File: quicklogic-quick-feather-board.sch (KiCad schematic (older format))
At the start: 50 parts, among them IC1 EOS-S3, J5 0473460001, Q1 BSS138AKA, Q2 BSS84, U1 TPS62821DLCR, U2 MCP73831T-2ACI_OT, U3 GD25Q16CWIGR, U4 DPS310, U5 MC3635, X1 ECS-_327-12_5-34B-TR

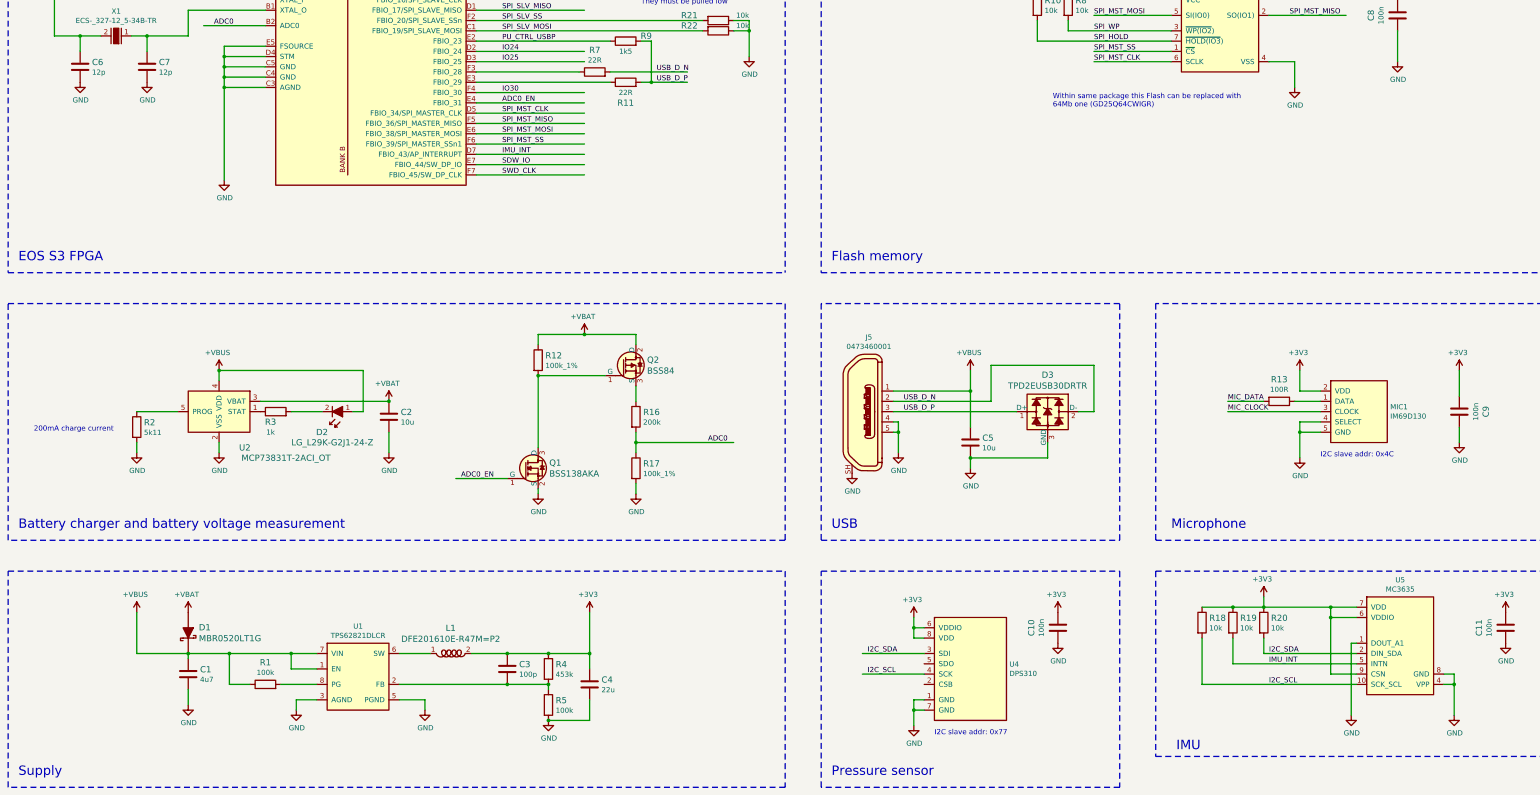
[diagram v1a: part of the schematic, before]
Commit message: Added remarks about power consuption, added filtering capactitors for EOS-S3
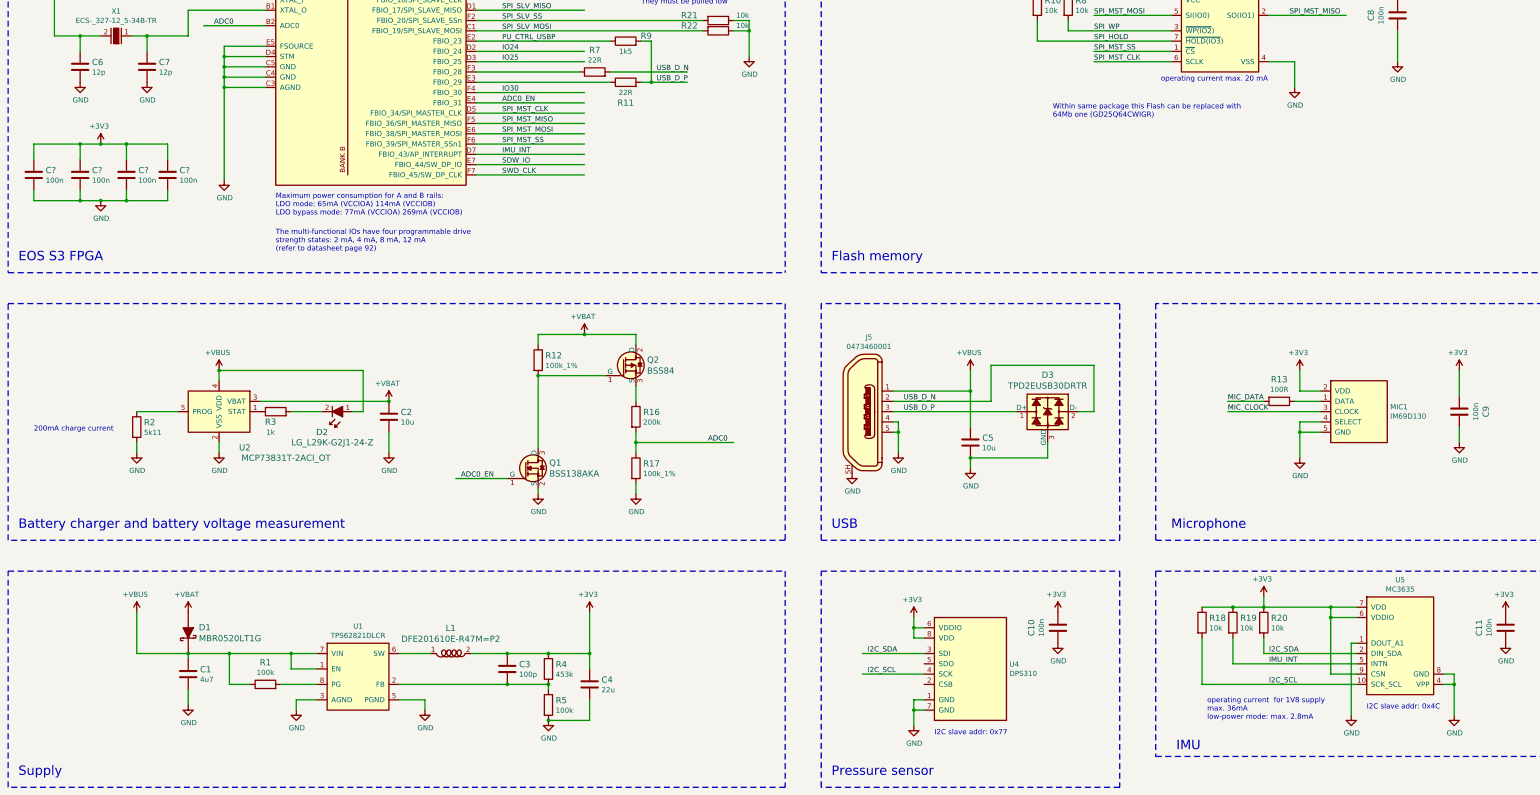
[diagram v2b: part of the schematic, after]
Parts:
- added C? (x4): C_100n_0402_6V3, antmicro-footprints:0402-cap, symbol antmicroCapacitors0402:C_100n_0402_6V3
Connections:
- wire segments 198 -> 214
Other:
- note added: "Maximum power consumption for A and B rails:\nLDO mode: 65mA (VCCIOA) 114mA (VCCIOB)\nLDO bypass mode: 77mA (VCCIOA) 269mA (VCCIOB)"
- note added: "The multi-functional IOs have four programmable drive \nstrength states: 2 mA, 4 mA, 8 mA, 12 mA \n(refer to datasheet page 92)"
- note added: "operating current for 1V8 supply\nmax. 36mA\nlow-power mode: max. 2.8mA"
- note added: "operating current max. 20 mA"
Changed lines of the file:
@@
 Wire Wire Line
 	11250 3050 12000 3050
-Text Notes 10850 3600 0    50   ~ 0
+Text Notes 10850 3700 0    50   ~ 0
 Within same package this Flash can be replaced with \n64Mb one (GD25Q64CWIGR)
 Wire Wire Line
@@
 Wire Wire Line
 	9600 9100 9000 9100
-Text Notes 13450 7000 0    50   ~ 0
+Text Notes 13900 9450 0    50   ~ 0
 I2C slave addr: 0x4C
 Text Notes 9700 9700 0    50   ~ 0
@@
 $EndComp
 Connection ~ 4400 6450
+Text Notes 3300 4650 0    50   ~ 0
+Maximum power consumption for A and B rails:\nLDO mode: 65mA (VCCIOA) 114mA (VCCIOB)\nLDO bypass mode: 77mA (VCCIOA) 269mA (VCCIOB)
+$Comp
+L antmicroCapacitors0402:C_100n_0402_6V3 C?
+U 1 1 5DDEA3A8
+P 950 4250
+F 0 "C?" H 1065 4295 60  0000 L CNN
+F 1 "C_100n_0402_6V3" H 950 4100 60  0001 C CNN
+F 2 "antmicro-footprints:0402-cap" H 1150 4450 60  0001 L CNN
+F 3 "" H 950 4250 50  0001 C CNN
+F 4 "Walsin" H 1150 4650 60  0001 L CNN "Manufacturer"
+F 5 "0402X104K6R3CT" H 1150 4550 60  0001 L CNN "MPN"
+F 6 "100n" H 1065 4197 50  0000 L CNN "Val"
+	1    950  4250
+	1    0    0    -1
+$EndComp
+$Comp
+L antmicroCapacitors0402:C_100n_0402_6V3 C?
+U 1 1 5DDEA7E7
+P 1400 4250
+F 0 "C?" H 1515 4295 60  0000 L CNN
+F 1 "C_100n_0402_6V3" H 1400 4100 60  0001 C CNN
+F 2 "antmicro-footprints:0402-cap" H 1600 4450 60  0001 L CNN
+F 3 "" H 1400 4250 50  0001 C CNN
+F 4 "Walsin" H 1600 4650 60  0001 L CNN "Manufacturer"
+F 5 "0402X104K6R3CT" H 1600 4550 60  0001 L CNN "MPN"
+F 6 "100n" H 1515 4197 50  0000 L CNN "Val"
+	1    1400 4250
+	1    0    0    -1
+$EndComp
+$Comp
+L antmicroCapacitors0402:C_100n_0402_6V3 C?
+U 1 1 5DDEACD8
+P 1850 4250
+F 0 "C?" H 1965 4295 60  0000 L CNN
+F 1 "C_100n_0402_6V3" H 1850 4100 60  0001 C CNN
+F 2 "antmicro-footprints:0402-cap" H 2050 4450 60  0001 L CNN
+F 3 "" H 1850 4250 50  0001 C CNN
+F 4 "Walsin" H 2050 4650 60  0001 L CNN "Manufacturer"
+F 5 "0402X104K6R3CT" H 2050 4550 60  0001 L CNN "MPN"
+F 6 "100n" H 1965 4197 50  0000 L CNN "Val"
+	1    1850 4250
+	1    0    0    -1
+$EndComp
+$Comp
+L antmicroCapacitors0402:C_100n_0402_6V3 C?
+U 1 1 5DDEB04F
+P 2250 4250
+F 0 "C?" H 2365 4295 60  0000 L CNN
+F 1 "C_100n_0402_6V3" H 2250 4100 60  0001 C CNN
+F 2 "antmicro-footprints:0402-cap" H 2450 4450 60  0001 L CNN
+F 3 "" H 2250 4250 50  0001 C CNN
+F 4 "Walsin" H 2450 4650 60  0001 L CNN "Manufacturer"
+F 5 "0402X104K6R3CT" H 2450 4550 60  0001 L CNN "MPN"
+F 6 "100n" H 2365 4197 50  0000 L CNN "Val"
+	1    2250 4250
+	1    0    0    -1
+$EndComp
+$Comp
+L quicklogic-quick-feather-board:GND #PWR?
+U 1 1 5DDEB6DD
+P 1600 4500
+F 0 "#PWR?" H 1600 4250 50  0001 C CNN
+F 1 "GND" H 1605 4327 50  0000 C CNN
+F 2 "" H 1600 4500 50  0001 C CNN
+F 3 "" H 1600 4500 50  0001 C CNN
+	1    1600 4500
+	1    0    0    -1
+$EndComp
+$Comp
+L quicklogic-quick-feather-board:+3V3 #PWR?
+U 1 1 5DDEBD0E
+P 1600 3900
+F 0 "#PWR?" H 1600 3900 50  0001 C CNN
+F 1 "+3V3" H 1585 4023 50  0000 C CNN
+F 2 "" H 1600 3900 50  0001 C CNN
+F 3 "" H 1600 3900 50  0001 C CNN
+	1    1600 3900
+	1    0    0    -1
+$EndComp
+Wire Wire Line
+	2250 4100 2250 3950
+Wire Wire Line
+	2250 3950 1850 3950
+Wire Wire Line
+	1850 4100 1850 3950
+Connection ~ 1850 3950
+Wire Wire Line
+	1850 3950 1600 3950
+Wire Wire Line
+	1600 3950 1400 3950
+Wire Wire Line
+	1400 3950 1400 4100
+Connection ~ 1600 3950
+Wire Wire Line
+	1400 3950 950  3950
+Wire Wire Line
+	950  3950 950  4100
+Connection ~ 1400 3950
+Wire Wire Line
+	950  4400 950  4500
+Wire Wire Line
+	950  4500 1400 4500
+Wire Wire Line
+	2250 4500 2250 4400
+Wire Wire Line
+	1850 4400 1850 4500
+Connection ~ 1850 4500
+Wire Wire Line
+	1850 4500 2250 4500
+Wire Wire Line
+	1400 4400 1400 4500
+Connection ~ 1400 4500
+Wire Wire Line
+	1400 4500 1600 4500
+Connection ~ 1600 4500
+Wire Wire Line
+	1600 4500 1850 4500
+Text Notes 3300 5000 0    50   ~ 0
+The multi-functional IOs have four programmable drive \nstrength states: 2 mA, 4 mA, 8 mA, 12 mA \n(refer to datasheet page 92)
+Text Notes 11900 3350 0    50   ~ 0
+operating current max. 20 mA
+Text Notes 12350 9550 0    50   ~ 0
+operating current  for 1V8 supply\nmax. 36mA\nlow-power mode: max. 2.8mA
 $EndSCHEMATC

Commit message: Updated naming
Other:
- note added: "Accelerometer"
- note added: "EOS S3"
- note removed: "EOS S3 FPGA"
- note removed: "IMU"
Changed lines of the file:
@@
 	2550 1550 2900 1550
 Text Notes 800  5100 0    91   ~ 0
-EOS S3 FPGA
+EOS S3
 Text Notes 800  7700 0    91   ~ 0
 Battery charger and battery voltage measurement
@@
 	11850 8100 11850 9900
 Text Notes 12050 9850 0    91   ~ 0
-IMU
+Accelerometer
 Text Label 5500 3550 0    50   ~ 0
 ADC0_EN
